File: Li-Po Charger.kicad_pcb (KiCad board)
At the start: 2 copper layers, 40 x 23 mm, 32 parts, among them J1 USB_C_Receptacle_PowerOnly_6P, J2 JST_2mm_LiPo, J3 I^{2}C 1, J4 I^{2}C 2, J5 I^{2}C 3, J6 Inputs, J7 Outputs, Q1 IRLML6401, U1 MAX17048, U2 ME6211C33M5, U3 TP4056-42-ESOP8

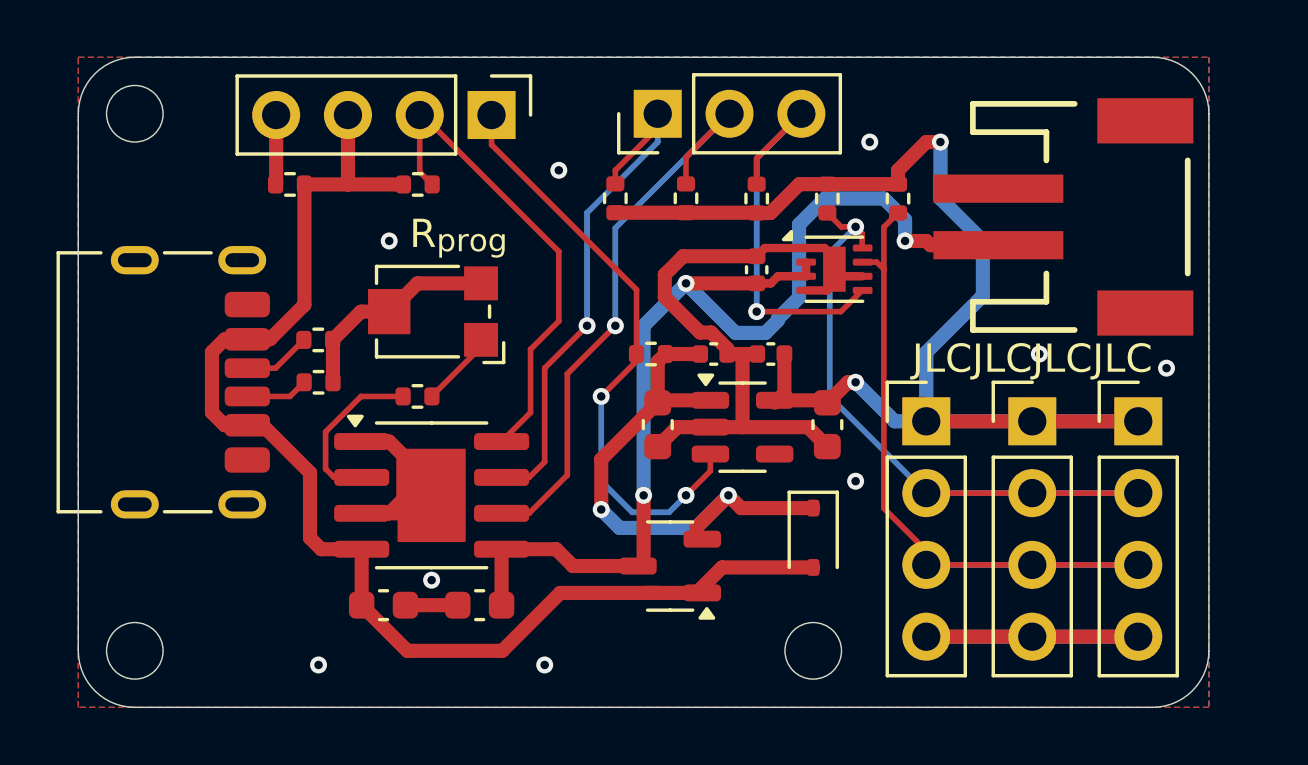
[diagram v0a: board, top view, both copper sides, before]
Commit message: Revise the board following a design review
With R1 at 10K the load ran through Q1's body diode for about 35 ms
after USB was unplugged; 1.5K shortens that to about 5 ms. A USB host
expects about 10 uF at plug-in, and C3 was the part of it that could
shrink. Plug-in ringing on VBUS reaches the LDO through D1, and the
LDO's 6.5 V limit is the lowest on that rail.

PWR_OFF and CHRG_OFF are pulled up, so the 3.3 V rail and charging are
on until a pin is driven low.

The LDO cannot feed an amplifier or a motor, which take V_SYS or the
battery from J8. A track running down to J8 on the back cuts the ground
pour that joins the USB side to the battery side, so the battery and
V_SYS reach it on the front and 5 V crosses on the back.

J2's mounting pad was inside the edge clearance. The board file is in
KiCad 10's format, which KiCad 9 cannot open.
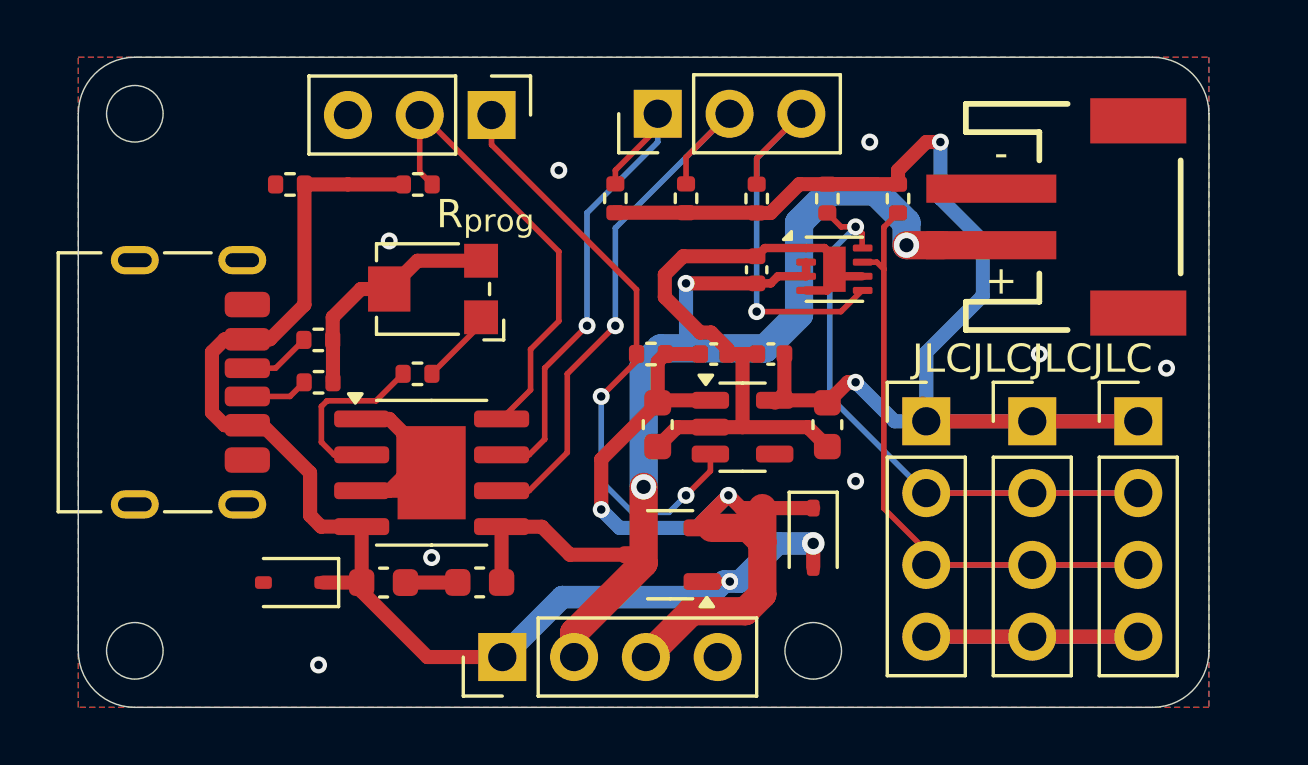
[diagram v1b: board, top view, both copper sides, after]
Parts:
- added D2: SD05, Diode_SMD:D_SOD-323, F.Cu at (167.6, 51.1)
- added J8: Power, Connector_PinHeader_2.54mm:PinHeader_1x04_P2.54mm_Vertical, F.Cu at (175.0, 53.7)
- C3: value 10uF -> 1uF
- J6: value Inputs -> Control; footprint Connector_PinHeader_2.54mm:PinHeader_1x04_P2.54mm_Vertical -> Connector_PinHeader_2.54mm:PinHeader_1x03_P2.54mm_Vertical
- J7: value Outputs -> Status
- R1: value 10K -> 1.5K
- moved G*** 1.60 mm to (170.9, 48.5)
- moved C7 0.80 mm to (174.2, 51.1)
- moved C6 0.80 mm to (170.8, 51.1)
- moved R11 0.80 mm to (172.0, 43.7)
- moved RV1 0.80 mm to (172.4, 40.7)
- moved U3 0.80 mm to (172.5, 47.2)
- moved Q1 0.40 mm to (180.9, 50.1)
- moved J2 0.25 mm to (196.0, 38.1)
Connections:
- net /CHARGE_EN renamed /~{CHRG_OFF}
- net /POWER_EN renamed /~{PWR_OFF}
- J6 pad 3: +5V -> GND
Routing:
- net /V_{SYS}: track 20.0 -> 29.6 mm
- net +BATT: track 39.4 -> 44.7 mm
- net GND: track 56.2 -> 54.5 mm, vias 9 -> 8
- net /~{CHARGING}: track 18.8 -> 18.0 mm
- net /~{READY}: track 21.2 -> 20.4 mm
- net /~{CHRG_OFF}: track 17.1 -> 16.3 mm
- net +5V: track 45.3 -> 45.8 mm, vias 0 -> 2
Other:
- board text added: "+"
- board text added: "-"
- board text added: "5V OUT"
- board text added: "VBAT"
- board text added: "VSYS"
- board text added: "~{CHRG_OFF}"
- board text added: "~{PWR_OFF}"
- board text removed: "+5V"
- board text removed: "~{CHRG_EN}"
- board text removed: "~{POWER_EN}"
